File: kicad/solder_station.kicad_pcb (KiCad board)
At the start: 2 copper layers, 33 parts, among them IC1 OPA336U, P2 POWER, P3 MCU, P4 KEYPAD, P5 JACK, SW1 SPST, SW2 SPST, SW3 SPST, SW4 SPST, SW5 ENC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

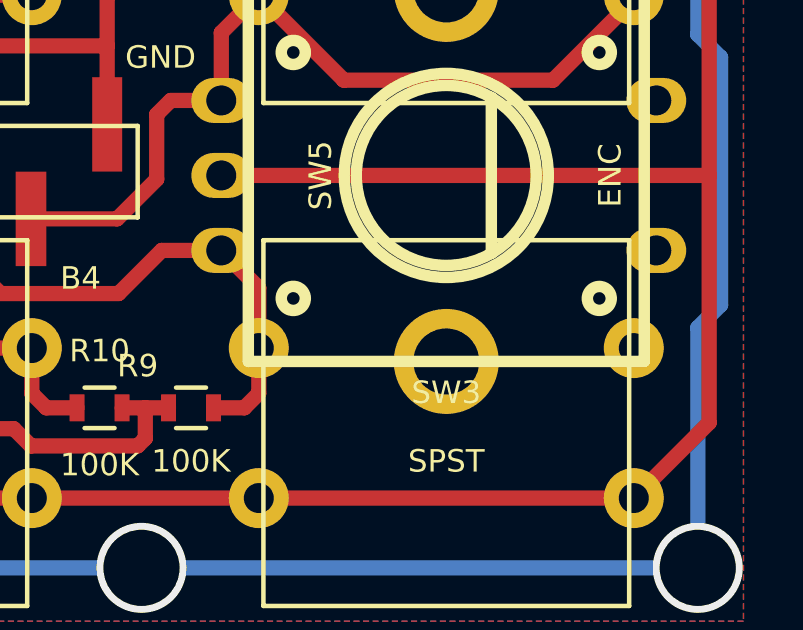
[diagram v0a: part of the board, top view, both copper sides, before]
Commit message: Add missing track
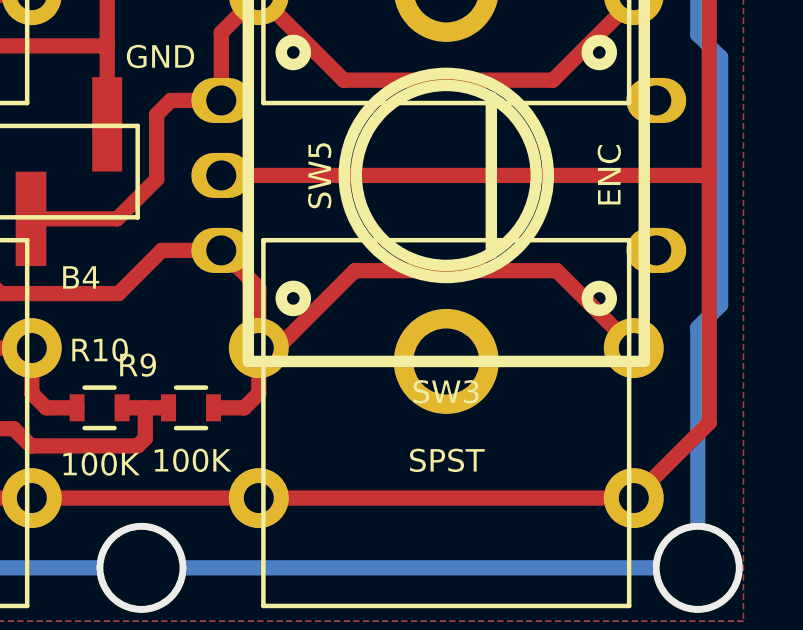
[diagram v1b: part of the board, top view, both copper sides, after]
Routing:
- net PIN_B3: track 21.2 -> 35.8 mm

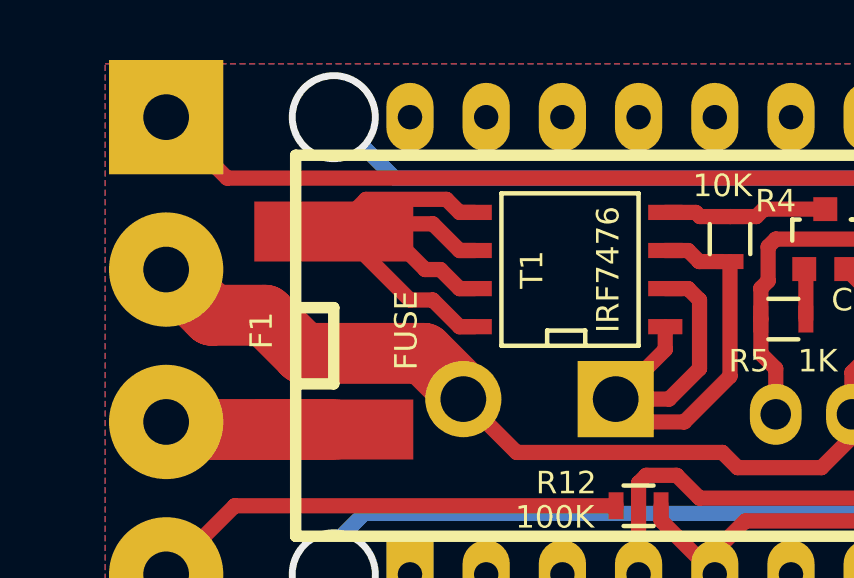
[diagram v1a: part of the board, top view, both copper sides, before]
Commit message: Rework pcb for iron toner transfer
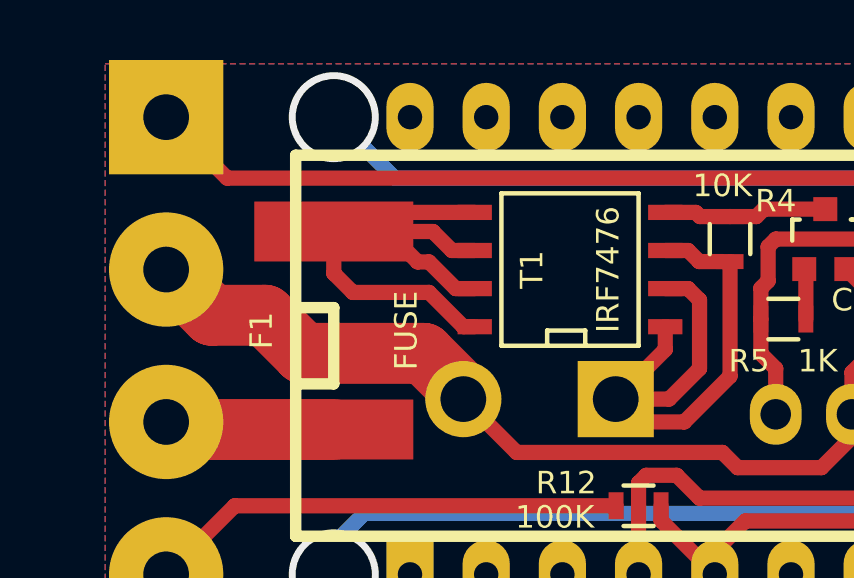
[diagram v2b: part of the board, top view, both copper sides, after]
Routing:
- net Net-(F1-Pad1): track 22.9 -> 25.4 mm

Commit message: Add via instead of go under resistors
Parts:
- moved R12 5.89 mm to (136.1, 100.3)
- moved R3 3.56 mm to (154.7, 90.6)
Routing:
- net MCU_STANDBY: track 16.7 -> 31.0 mm, vias 0 -> 2
- net STANDBY: track 15.9 -> 10.4 mm
- net Net-(C1-Pad1): track 9.77 -> 15.1 mm
- net SENSOR: track 32.3 -> 28.7 mm
- net MCU_HEATER: track 23.5 -> 20.7 mm, vias 0 -> 2
- net MCU_SENSOR: track 20.5 -> 18.8 mm

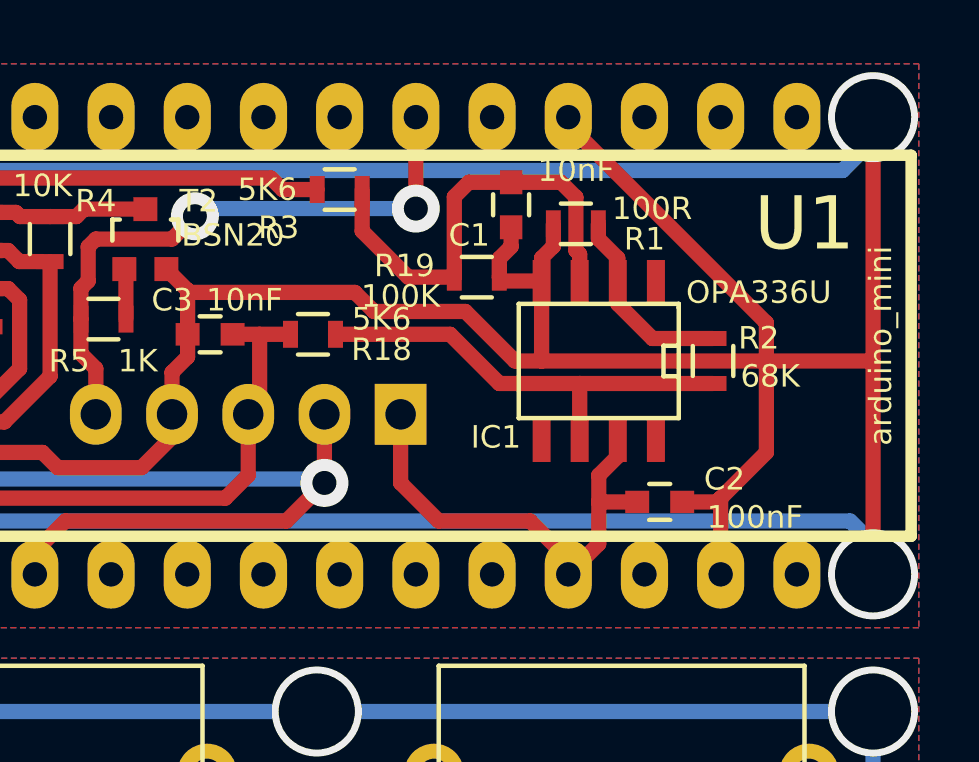
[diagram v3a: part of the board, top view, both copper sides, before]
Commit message: Add via instead of go under resistors
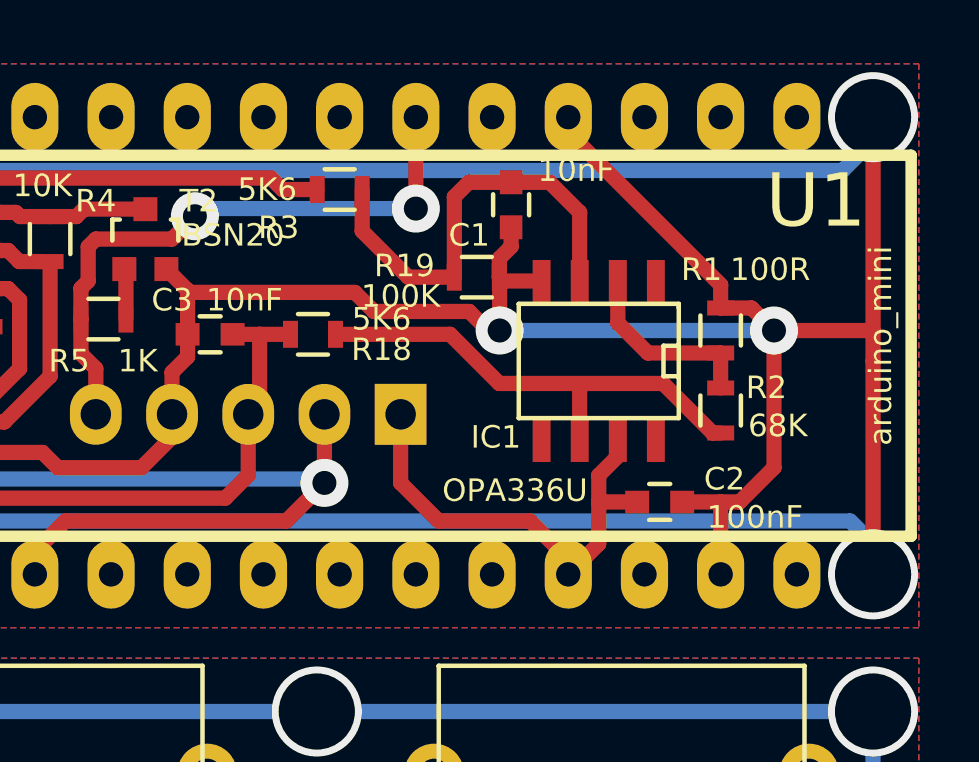
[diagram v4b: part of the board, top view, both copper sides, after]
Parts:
- moved R1 5.99 mm to (167.4, 95.2), turned to 90 degrees
- moved R2 1.67 mm to (167.4, 97.9)
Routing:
- net GND: track 187.0 -> 185.1 mm, vias 4 -> 6
- net Net-(IC1-Pad6): track 15.2 -> 16.1 mm

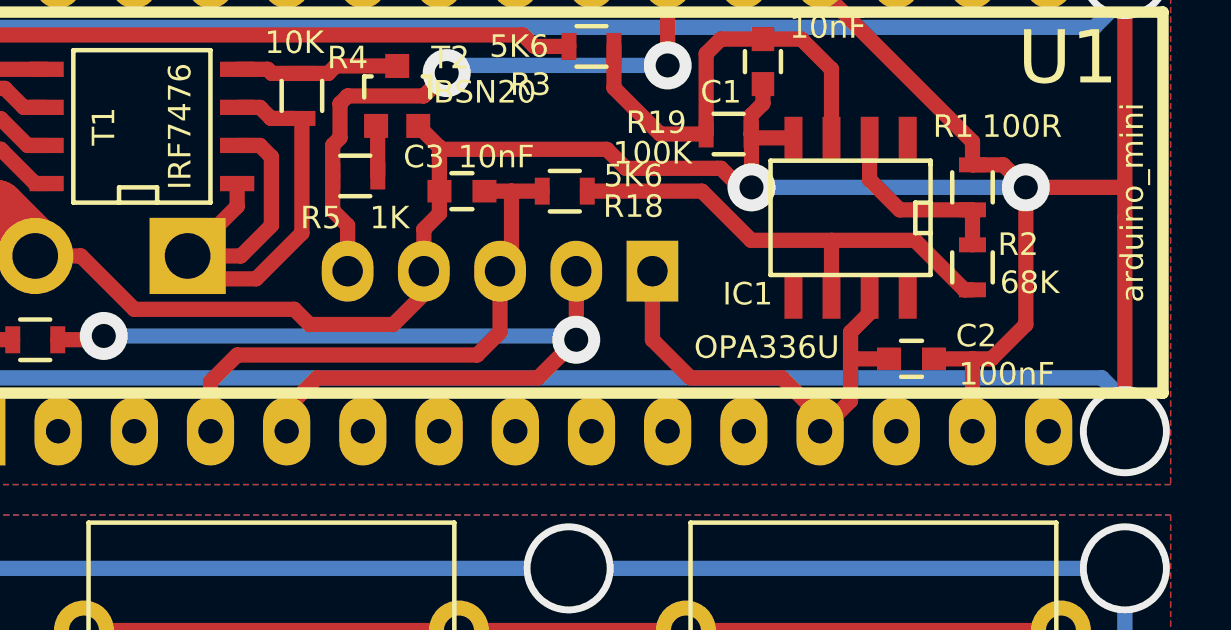
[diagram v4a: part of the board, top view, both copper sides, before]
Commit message: Add VIN jumper
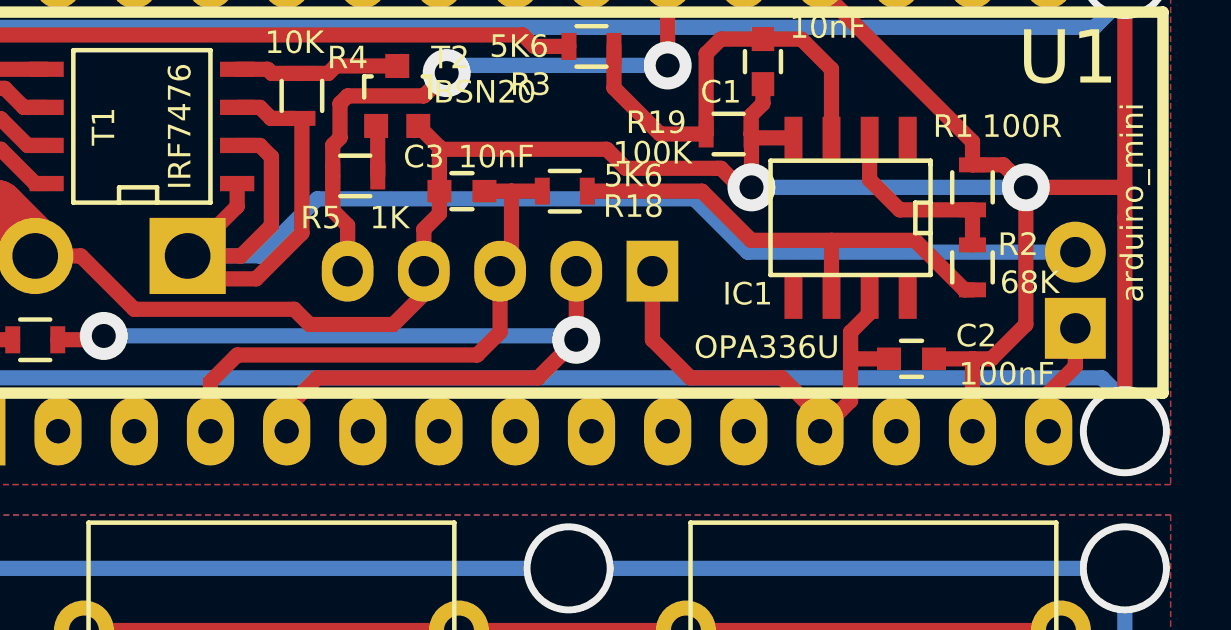
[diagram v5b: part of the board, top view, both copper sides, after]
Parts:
- added JP1: JUMPER, Pin_Headers:Pin_Header_Straight_1x02, B.Cu at (170.8, 99.9)
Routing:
- net +12V: track 20.5 -> 51.7 mm
- net Net-(JP1-Pad1): track 0.00 -> 3.80 mm
